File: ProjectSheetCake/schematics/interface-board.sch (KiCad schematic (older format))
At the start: 46 parts, among them P1 CONN_8, P2 CONN_6, P3 CONN_8, P4 CONN_6, P7 X_Y_SERVO, P8 Z_A_SERVO

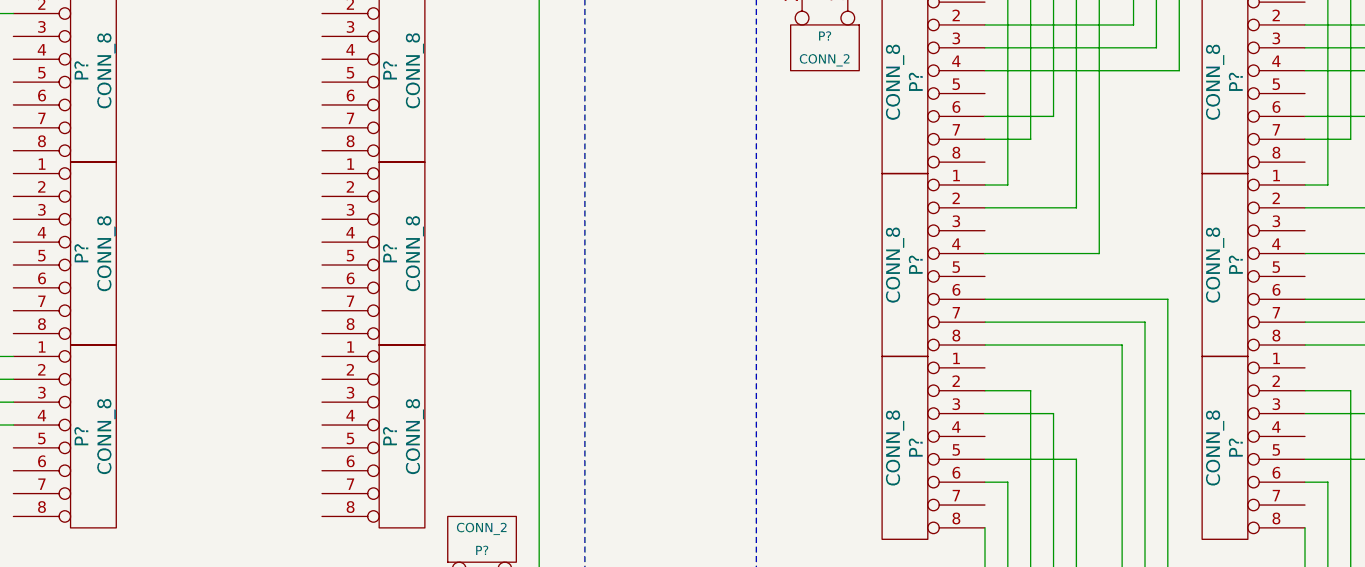
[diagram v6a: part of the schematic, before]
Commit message: updated to put Mesa board names
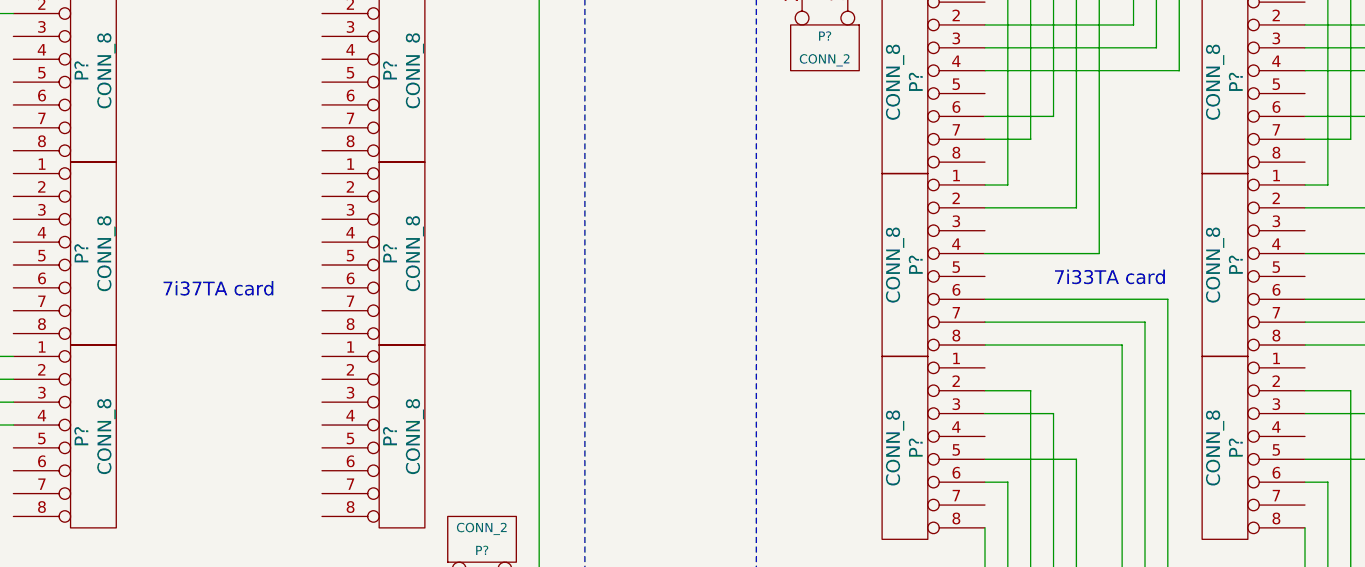
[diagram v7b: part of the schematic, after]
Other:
- note added: "7i33TA card"
- note added: "7i37TA card"
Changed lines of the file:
@@
-EESchema Schematic File Version 2  date 8/16/2011 9:09:40 PM
+EESchema Schematic File Version 2  date 8/16/2011 9:52:24 PM
 LIBS:power
 LIBS:device
@@
 Comment4 ""
 $EndDescr
+Text Notes 9400 5450 0    60   ~ 0
+7i33TA card
+Text Notes 5500 5500 0    60   ~ 0
+7i37TA card
 Wire Wire Line
 	4850 4150 4600 4150

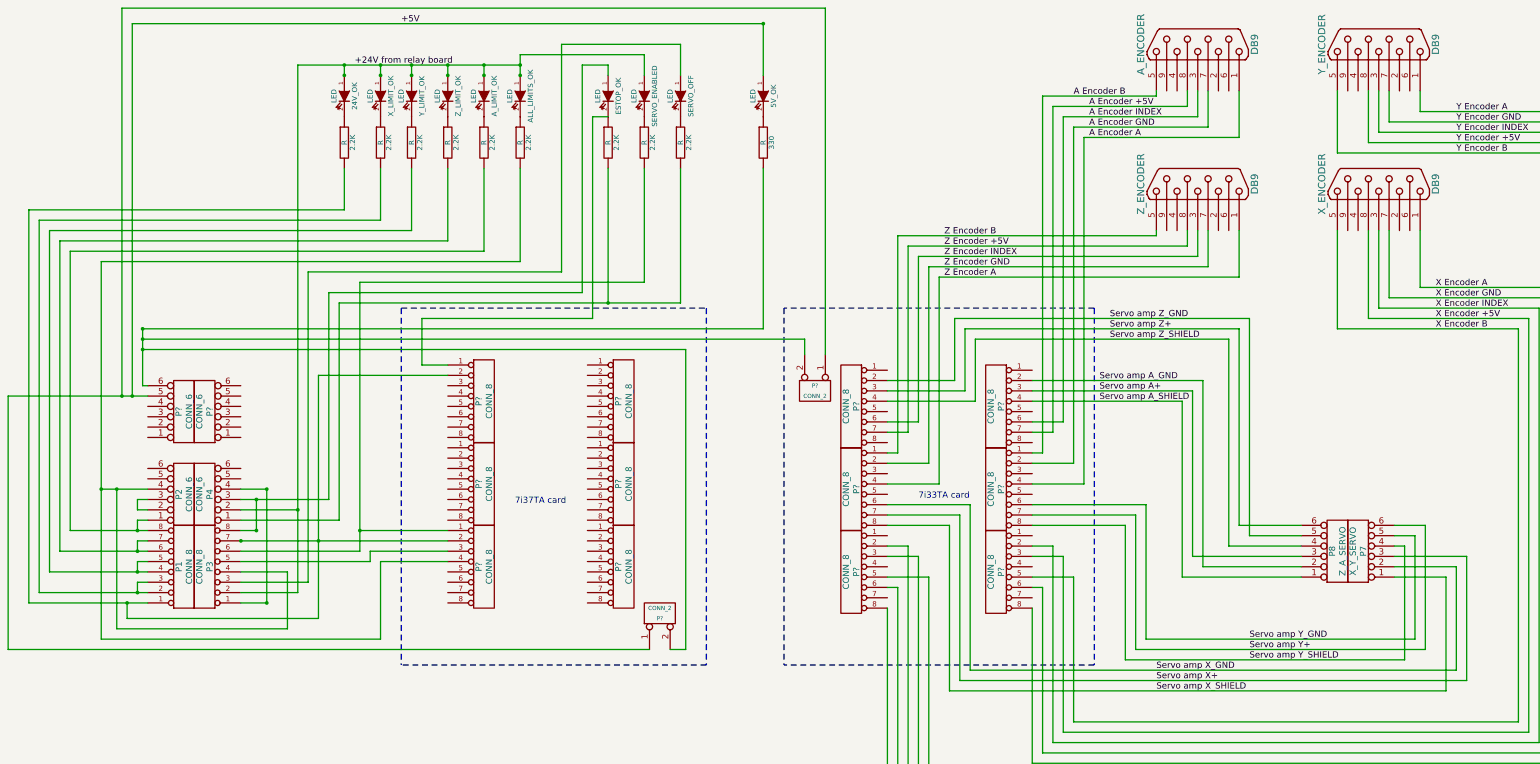
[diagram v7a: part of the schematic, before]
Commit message: fixed X and Y signals wrong, and removed 5V circuit
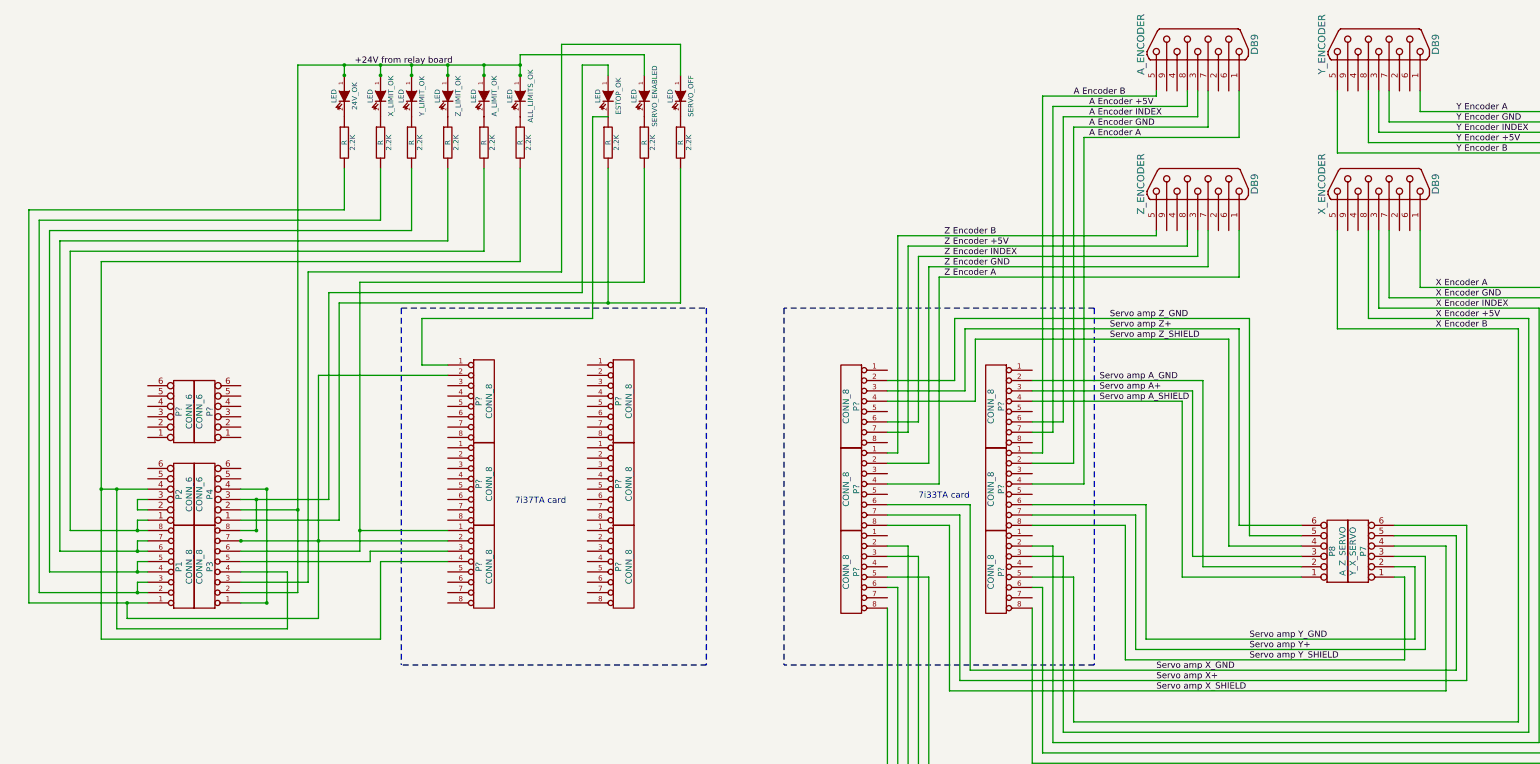
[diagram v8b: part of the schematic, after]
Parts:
- removed 330: R, symbol R
- removed 5V_OK: LED, symbol LED
- removed P? (x2): CONN_2, symbol CONN_2
- P7: value X_Y_SERVO -> Y_X_SERVO
- P8: value Z_A_SERVO -> A_Z_SERVO
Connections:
- net labels removed: +5V
- wire segments 265 -> 247
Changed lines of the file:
@@
-EESchema Schematic File Version 2  date 8/16/2011 9:52:24 PM
+EESchema Schematic File Version 2  date 8/18/2011 9:59:23 PM
 LIBS:power
 LIBS:device
@@
 Sheet 1 1
 Title ""
-Date "17 aug 2011"
+Date "19 aug 2011"
 Rev ""
 Comp ""
@@
 Comment4 ""
 $EndDescr
-Text Notes 9400 5450 0    60   ~ 0
-7i33TA card
-Text Notes 5500 5500 0    60   ~ 0
-7i37TA card
+Wire Wire Line
+	14500 5900 14500 7300
+Wire Wire Line
+	14700 5700 14700 7200
+Wire Wire Line
+	14200 6100 14200 6800
 Wire Wire Line
 	4850 4150 4600 4150
@@
 Wire Notes Line
 	11100 3600 8100 3600
-Wire Wire Line
-	8500 700  1700 700
 Wire Notes Line
 	4400 3600 7350 3600
@@
 	6750 3350 6750 2250
 Wire Wire Line
-	1900 3800 7900 3800
-Wire Wire Line
-	1900 4000 7150 4000
-Wire Wire Line
-	7900 850  1800 850
-Connection ~ 1800 4450
-Wire Wire Line
-	1950 4450 600  4450
-Wire Wire Line
-	600  4450 600  6900
-Wire Wire Line
-	600  6900 6800 6900
-Wire Wire Line
-	8300 4050 8300 3900
-Wire Wire Line
-	1900 3800 1900 4350
-Wire Wire Line
-	7900 3800 7900 2250
-Connection ~ 1900 3800
-Wire Wire Line
-	1900 4350 1950 4350
-Wire Wire Line
 	1750 6600 3600 6600
 Connection ~ 2850 5850
@@
 	11600 5500 10500 5500
 Wire Wire Line
-	14300 6900 11500 6900
-Wire Wire Line
-	14200 5800 14200 6800
+	11500 6900 14300 6900
 Wire Wire Line
 	10500 5700 11400 5700
@@
 	15600 3400 14250 3400
 Wire Wire Line
-	14000 5700 14300 5700
+	14000 6000 14300 6000
 Wire Wire Line
 	11400 5700 11400 7000
 Wire Wire Line
-	14100 5900 14100 7000
-Wire Wire Line
-	14100 5900 14000 5900
+	14000 6200 14100 6200
 Wire Wire Line
 	9900 7100 9900 5500
@@
 	9900 7100 14600 7100
 Wire Wire Line
-	14600 7100 14600 6100
-Wire Wire Line
-	14600 6100 14000 6100
-Wire Wire Line
-	14000 6000 14700 6000
-Wire Wire Line
-	14700 6000 14700 7200
+	14000 5800 14600 5800
+Wire Wire Line
+	14700 5700 14000 5700
 Wire Wire Line
 	14700 7200 9800 7200
@@
 	9800 7200 9800 5600
 Wire Wire Line
-	14000 6200 14500 6200
-Wire Wire Line
-	14500 6200 14500 7300
+	14500 5900 14000 5900
 Wire Wire Line
 	14500 7300 9700 7300
@@
 	9700 7300 9700 5700
 Wire Wire Line
-	14200 5800 14000 5800
+	14200 6100 14000 6100
 Wire Wire Line
 	10500 6300 10600 6300
@@
 	9900 5500 9100 5500
 Wire Wire Line
-	14100 7000 11400 7000
-Wire Wire Line
-	14200 6800 11600 6800
-Wire Wire Line
-	14300 5700 14300 6900
+	11400 7000 14100 7000
+Wire Wire Line
+	11600 6800 14200 6800
 Wire Wire Line
 	11500 6900 11500 5600
@@
 Wire Wire Line
 	7100 1050 7100 1350
-Wire Wire Line
-	7900 850  7900 1350
-Wire Wire Line
-	1800 850  1800 4450
-Connection ~ 7900 850
-Connection ~ 1900 3900
-Wire Wire Line
-	7150 4000 7150 6900
-Wire Wire Line
-	8500 700  8500 4050
-Wire Wire Line
-	1700 700  1700 4450
-Connection ~ 1700 4450
-Connection ~ 1900 4000
-Wire Wire Line
-	7150 6900 7000 6900
 Wire Wire Line
 	6750 1150 5550 1150
@@
 Wire Notes Line
 	7350 7050 4400 7050
-Wire Wire Line
-	8300 3900 1900 3900
 Wire Notes Line
 	8100 3600 8100 7050
@@
 Wire Wire Line
 	3600 4250 4850 4250
-$Comp
-L CONN_2 P?
-U 1 1 4E460210
-P 6900 6550
-F 0 "P?" V 6850 6550 40  0000 C CNN
-F 1 "CONN_2" V 6950 6550 40  0000 C CNN
-	1    6900 6550
-	0    -1   -1   0
-$EndComp
-$Comp
-L CONN_2 P?
-U 1 1 4E4601E7
-P 8400 4400
-F 0 "P?" V 8350 4400 40  0000 C CNN
-F 1 "CONN_2" V 8450 4400 40  0000 C CNN
-	1    8400 4400
-	0    1    1    0
-$EndComp
-Text Label 4400 850  0    60   ~ 0
-+5V
+Wire Wire Line
+	14300 6000 14300 6900
+Wire Wire Line
+	14100 7000 14100 6200
+Wire Wire Line
+	14600 5800 14600 7100
+Text Notes 9400 5450 0    60   ~ 0
+7i33TA card
+Text Notes 5500 5500 0    60   ~ 0
+7i37TA card
 Text Label 11250 3900 0    60   ~ 0
 Servo amp Z_SHIELD
@@
 $EndComp
 $Comp
-L R 330
-U 1 1 4E45E288
-P 7900 2000
-F 0 "330" V 7980 2000 50  0000 C CNN
-F 1 "R" V 7900 2000 50  0000 C CNN
-	1    7900 2000
-	1    0    0    -1
-$EndComp
-$Comp
-L LED 5V_OK
-U 1 1 4E45E287
-P 7900 1550
-F 0 "5V_OK" H 7900 1650 50  0000 C CNN
-F 1 "LED" H 7900 1450 50  0000 C CNN
-	1    7900 1550
-	0    1    1    0
-$EndComp
-$Comp
 L LED ESTOP_OK
 U 1 1 4E45E280
@@
 P 13650 5950
 F 0 "P7" V 13600 5950 60  0000 C CNN
-F 1 "X_Y_SERVO" V 13700 5950 60  0000 C CNN
+F 1 "Y_X_SERVO" V 13700 5950 60  0000 C CNN
 	1    13650 5950
 	-1   0    0    1
@@
 P 13450 5950
 F 0 "P8" V 13400 5950 60  0000 C CNN
-F 1 "Z_A_SERVO" V 13500 5950 60  0000 C CNN
+F 1 "A_Z_SERVO" V 13500 5950 60  0000 C CNN
 	1    13450 5950
 	1    0    0    1
